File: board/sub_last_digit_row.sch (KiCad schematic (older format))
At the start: 83 parts, among them Q901 Q_PMOS_GSD, Q902 Q_PMOS_GSD, Q903 Q_PMOS_GSD, Q904 Q_PMOS_GSD, Q905 Q_PMOS_GSD, Q906 Q_PMOS_GSD, Q907 Q_PMOS_GSD, Q908 Q_PMOS_GSD, U901 TPIC6D595, U902 TPIC6D595, U903 TPIC6D595

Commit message: More Schematic progress
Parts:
- removed D904: (no value), symbol quokka:14-segment
- removed Q908: Q_PMOS_GSD, symbol Device:Q_PMOS_GSD
- removed R901, R902, R904, R905, R907, R908, R909, R910, R911, R912, R913, R914, R915, R916, R917, R918, R919, R921, R922, R924, R925, R926, R927, R928, R929, R930, R931, R932, R933, R934, R935, R936, R938, R939, R941, R942, R943, R944, R945, R946, R947, R948, R949, R950, R951, R952, R953, R955, R956, R958, R959, R960, R961, R962, R963, R964, R965, R966, R967, R968: 100, symbol Device:R
- removed R957: 4K7, symbol Device:R
- added C801, C802, C803: 1u, symbol Device:C
- added D804, D805, D806, D807, D808, D809, D810, D811, D812, D813, D814, D815, D816, D817, D818, D819: LED_Small, symbol Device:LED_Small
- added R808, R809, R810, R811, R812, R813, R814, R815, R816, R817, R818, R819, R820, R821, R822, R823, R824, R825, R826, R827, R828, R829, R830, R831, R832, R833, R834, R835, R836, R837, R838, R839, R840, R841, R842, R843, R844, R845, R846, R847, R848, R849, R850, R851, R852, R853, R854, R855, R856, R857, R858, R859, R860, R861, R862, R863, R864, R865, R866, R867, R868: 100, symbol Device:R
- renumbered D901 to D801, D902 to D802, D903 to D803, Q901 to Q801, Q902 to Q802, Q903 to Q803, Q904 to Q804, Q905 to Q805, Q906 to Q806, Q907 to Q807, R903 to R801, R906 to R802, R920 to R803, R923 to R804, R937 to R805, R940 to R806, R954 to R807, U901 to U801, U902 to U802, U903 to U803
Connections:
- net +5V: now also C801.1, C802.1, C803.1
- net GND: now also C801.2, C802.2, C803.2
- net at D801.1 (E): now also R808.1
- net at D801.10 (B): now also R816.1
- net at D801.12 (A): now also R817.1
- net at D801.13 (G1): now also R818.1
- net at D801.14 (K): now also R819.1
- net at D801.15 (J): now also R820.1
- net at D801.17 (H): now also R821.1
- net at D801.18 (F): now also R822.1
- net at D801.2 (N): now also R809.1
- net at D801.4 (M): now also R810.1
- net at D801.5 (L): now also R811.1
- net at D801.6 (G2): now also R812.1
- net at D801.7 (D): now also R813.1
- net at D801.8 (DP): now also R814.1
- net at D801.9 (C): now also R815.1
- net at U802.3 (DRAIN0): now also R808.2, R823.2, R838.2, R853.2
- net at U802.4 (DRAIN1): now also R809.2, R824.2, R839.2, R854.2
- net at U802.5 (DRAIN2): now also R810.2, R825.2, R840.2, R855.2
- net at U802.6 (DRAIN3): now also R811.2, R826.2, R841.2, R856.2
- net at U802.11 (DRAIN4): now also R812.2, R827.2, R842.2, R857.2
- net at U802.12 (DRAIN5): now also R813.2, R828.2, R843.2, R858.2
- net at U802.13 (DRAIN6): now also R814.2, R829.2, R844.2, R859.2
- net at U802.14 (DRAIN7): now also R815.2, R830.2, R845.2, R860.2
- net at U803.3 (DRAIN0): now also R816.2, R831.2, R846.2, R861.2
- net at U803.4 (DRAIN1): now also R817.2, R832.2, R847.2, R862.2
- net at U803.5 (DRAIN2): now also R818.2, R833.2, R848.2, R863.2
- net at U803.6 (DRAIN3): now also R819.2, R834.2, R849.2, R864.2
- net at U803.11 (DRAIN4): now also R820.2, R835.2, R850.2, R865.2
- net at U803.12 (DRAIN5): now also R821.2, R836.2, R851.2, R866.2
- net at U803.13 (DRAIN6): now also R822.2, R837.2, R852.2, R867.2
- net at D802.1 (E): now also R823.1
- net at D802.10 (B): now also R831.1
- net at D802.12 (A): now also R832.1
- net at D802.13 (G1): now also R833.1
- net at D802.14 (K): now also R834.1
- net at D802.15 (J): now also R835.1
- net at D802.17 (H): now also R836.1
- net at D802.18 (F): now also R837.1
- net at D802.2 (N): now also R824.1
- net at D802.4 (M): now also R825.1
- net at D802.5 (L): now also R826.1
- net at D802.6 (G2): now also R827.1
- net at D802.7 (D): now also R828.1
- net at D802.8 (DP): now also R829.1
- net at D802.9 (C): now also R830.1
- net at D803.1 (E): now also R838.1
- net at D803.10 (B): now also R846.1
- net at D803.12 (A): now also R847.1
- net at D803.13 (G1): now also R848.1
- net at D803.14 (K): now also R849.1
- net at D803.15 (J): now also R850.1
- net at D803.17 (H): now also R851.1
- net at D803.18 (F): now also R852.1
- net at D803.2 (N): now also R839.1
- net at D803.4 (M): now also R840.1
- net at D803.5 (L): now also R841.1
- net at D803.6 (G2): now also R842.1
- net at D803.7 (D): now also R843.1
- net at D803.8 (DP): now also R844.1
- net at D803.9 (C): now also R845.1
- net at Q807.2 (S): now also D804.2 (A), D805.2 (A), D806.2 (A), D807.2 (A), D808.2 (A), D809.2 (A), D810.2 (A), D811.2 (A), D812.2 (A), D813.2 (A), D814.2 (A), D815.2 (A), D816.2 (A), D817.2 (A), D818.2 (A), D819.2 (A)
- net at U803.14 (DRAIN7): now also R868.2
- net at U801.3 (DRAIN0): now also Q807.1 (G), R807.2, U801.4 (DRAIN1)
- new net: D804.1 (K), R853.1
- new net: D805.1 (K), R854.1
- new net: D806.1 (K), R855.1
- new net: D807.1 (K), R856.1
- new net: D808.1 (K), R857.1
- new net: D809.1 (K), R858.1
- new net: D810.1 (K), R859.1
- new net: D811.1 (K), R860.1
- new net: D812.1 (K), R861.1
- new net: D813.1 (K), R862.1
- new net: D814.1 (K), R863.1
- new net: D815.1 (K), R864.1
- new net: D816.1 (K), R865.1
- new net: D817.1 (K), R866.1
- new net: D818.1 (K), R867.1
- new net: D819.1 (K), R868.1
- no-connect marks 0 -> 1
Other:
- moved on the sheet: D801, D802, D803, Q801, Q802, Q803, Q804, Q805, Q806, Q807, R801, R802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

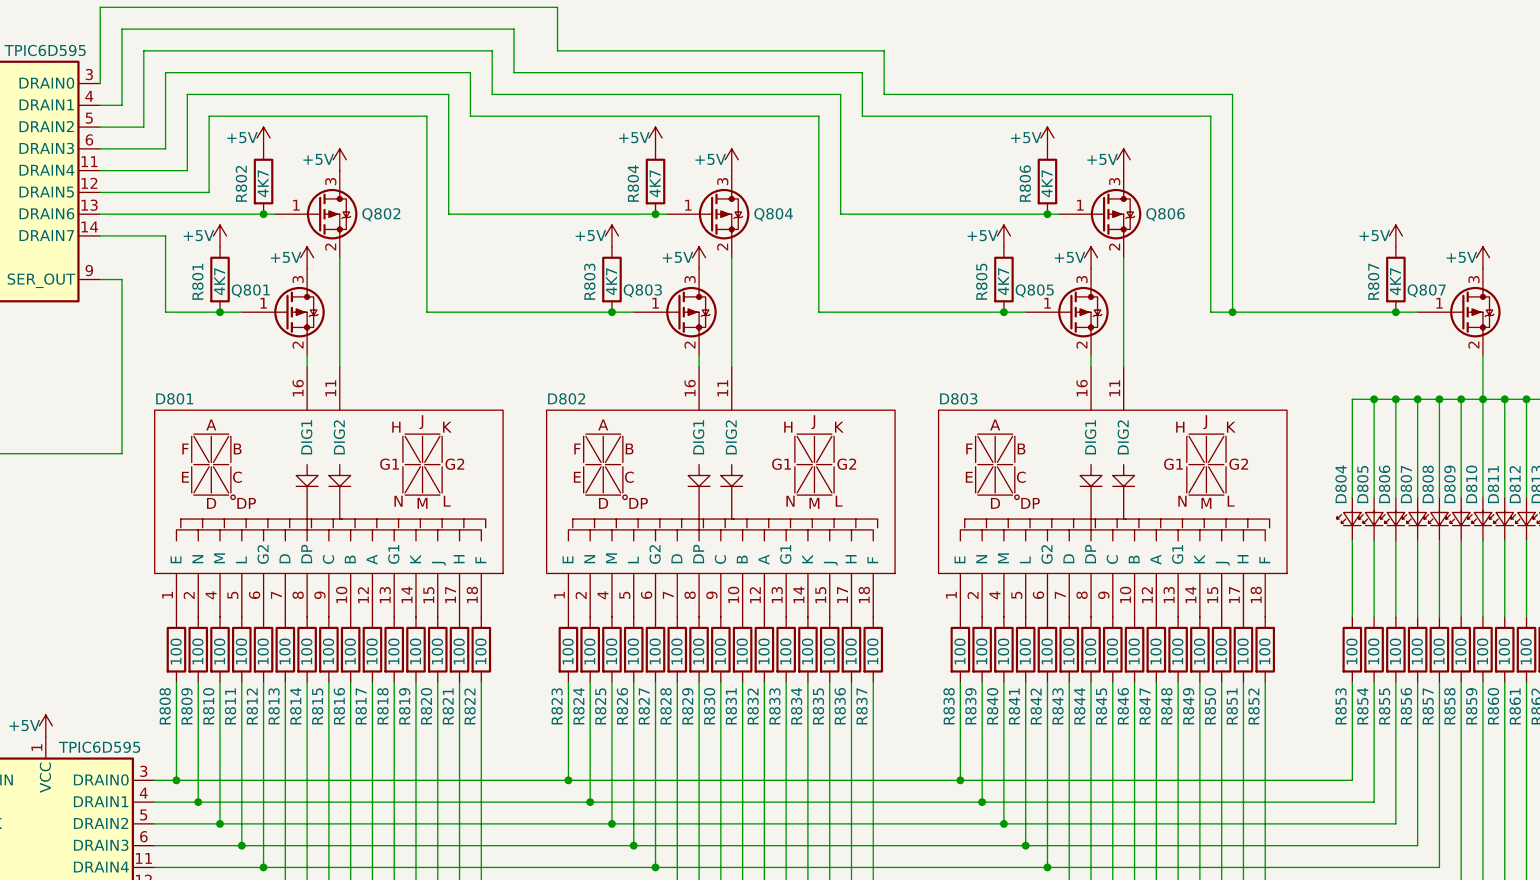
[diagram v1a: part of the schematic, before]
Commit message: Bus signal connectivity rebuilt
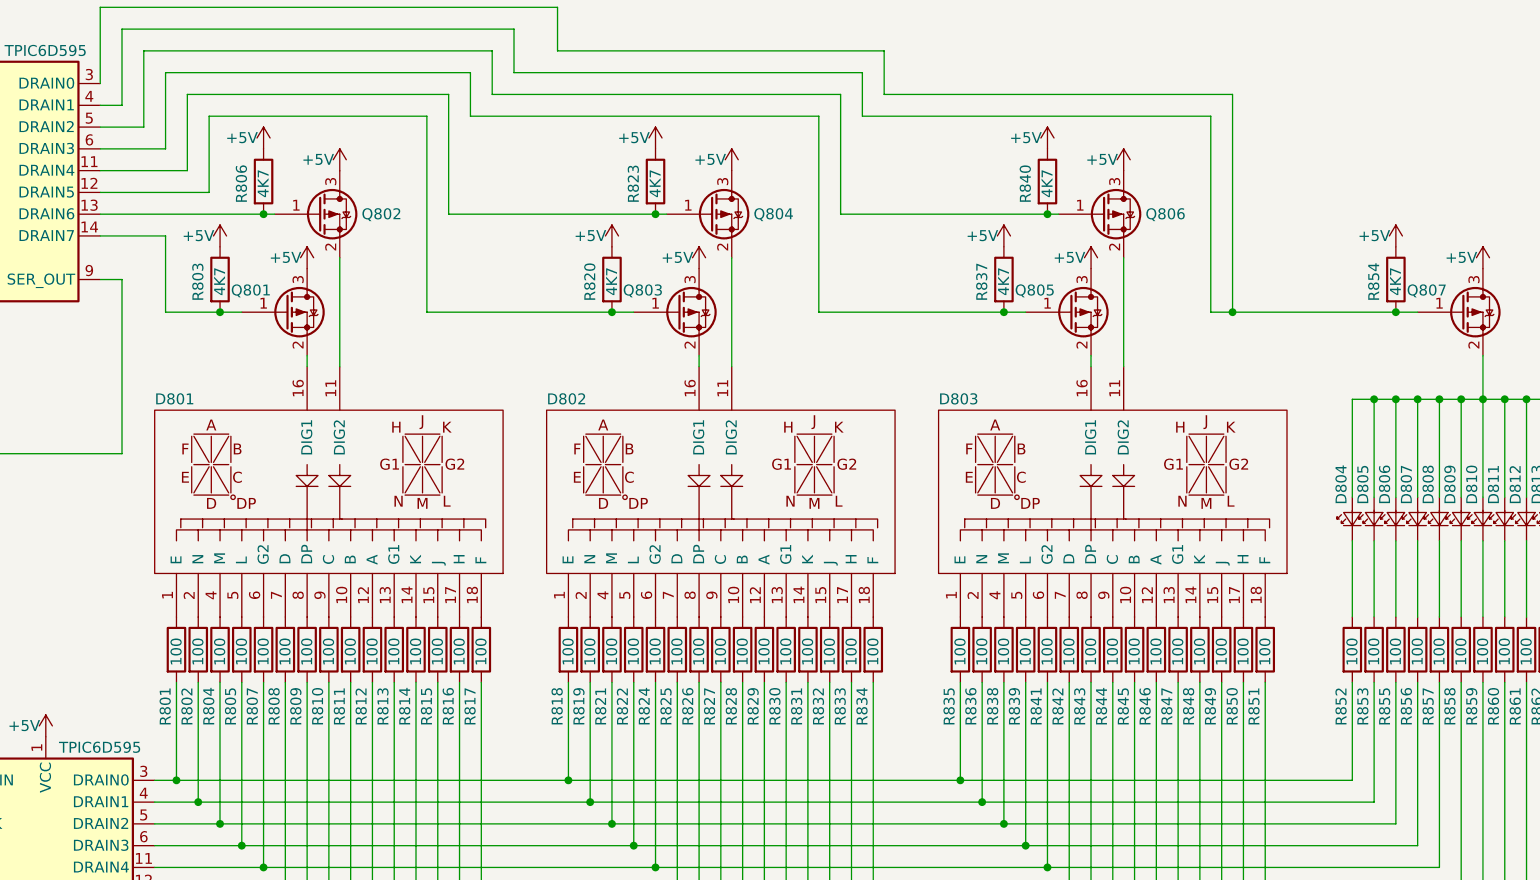
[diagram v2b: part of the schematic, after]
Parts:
- renumbered R808 to R801, R809 to R802, R801 to R803, R810 to R804, R811 to R805, R802 to R806, R812 to R807, R813 to R808, R814 to R809, R815 to R810, R816 to R811, R817 to R812, R818 to R813, R819 to R814, R820 to R815, R821 to R816, R822 to R817, R823 to R818, R824 to R819, R803 to R820, R825 to R821, R826 to R822, R804 to R823, R827 to R824, R828 to R825, R829 to R826, R830 to R827, R831 to R828, R832 to R829, R833 to R830, R834 to R831, R835 to R832, R836 to R833, R837 to R834, R838 to R835, R839 to R836, R805 to R837, R840 to R838, R841 to R839, R806 to R840, R842 to R841, R843 to R842, R844 to R843, R845 to R844, R846 to R845, R847 to R846, R848 to R847, R849 to R848, R850 to R849, R851 to R850, R852 to R851, R853 to R852, R854 to R853, R807 to R854

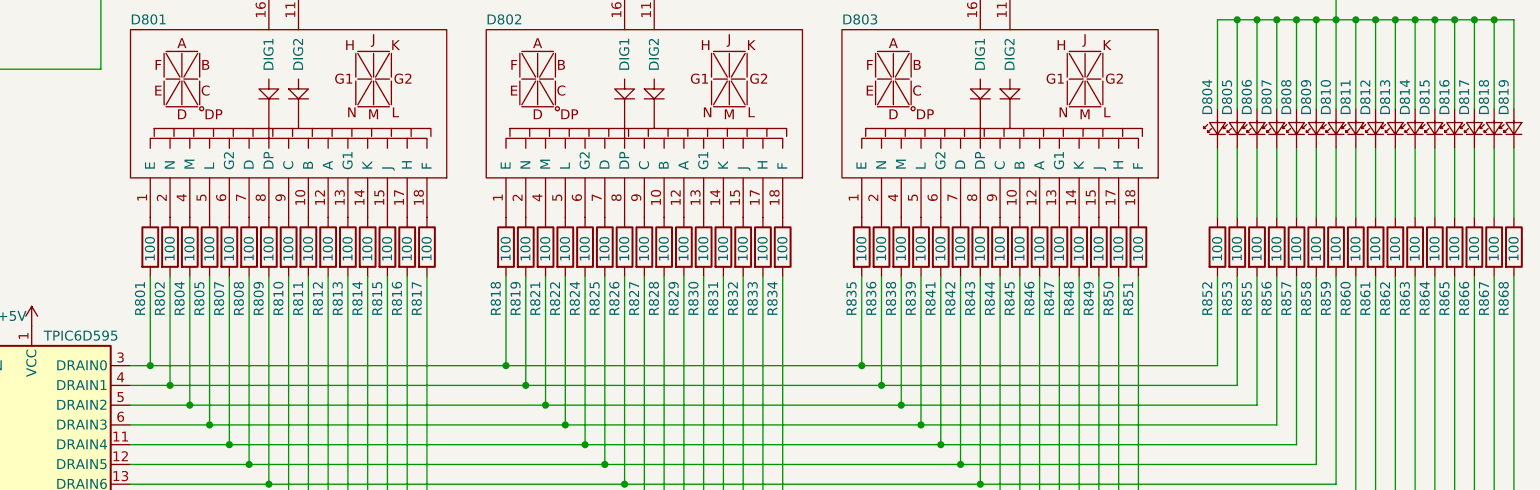
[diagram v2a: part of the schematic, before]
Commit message: made some changes based on projected power budget
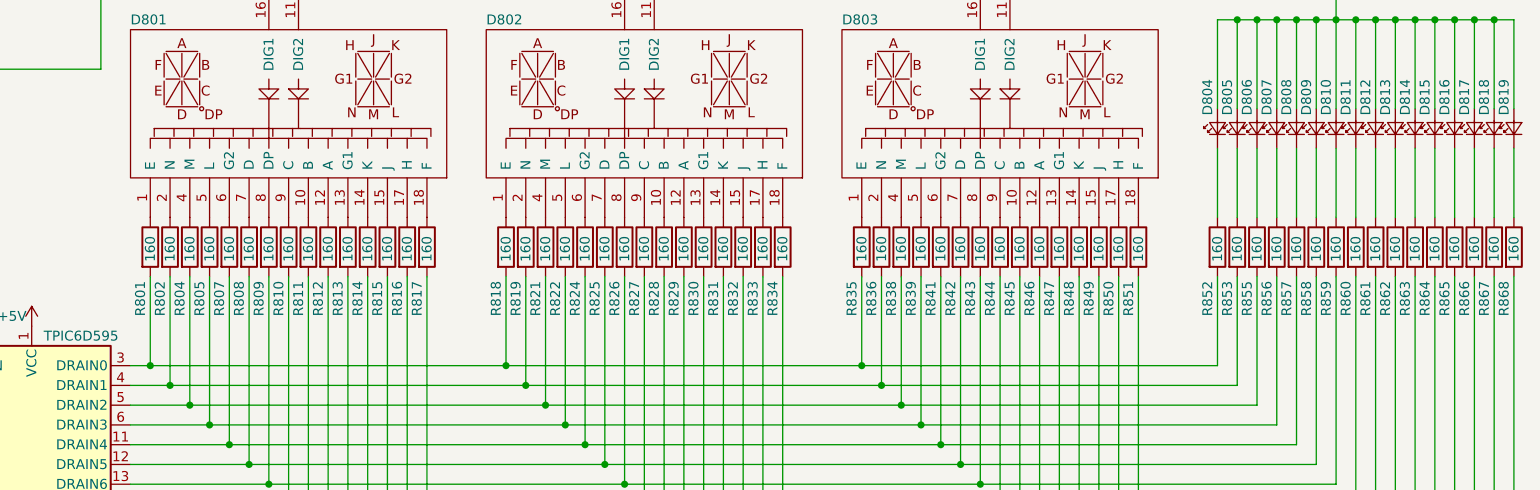
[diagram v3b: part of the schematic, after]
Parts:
- R801, R802, R804, R805, R807, R808, R809, R810, R811, R812, R813, R814, R815, R816, R817, R818, R819, R821, R822, R824, R825, R826, R827, R828, R829, R830, R831, R832, R833, R834, R835, R836, R838, R839, R841, R842, R843, R844, R845, R846, R847, R848, R849, R850, R851, R852, R853, R855, R856, R857, R858, R859, R860, R861, R862, R863, R864, R865, R866, R867, R868: value 100 -> 160

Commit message: Schematics mostly complete
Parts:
- renumbered D804 to D801, D805 to D802, D806 to D803, D807 to D804, D808 to D805, D809 to D806, D810 to D807, D811 to D808, D812 to D809, D813 to D810, D814 to D811, D815 to D812, D816 to D813, D817 to D814, D818 to D815, D819 to D816, D801 to D817, D802 to D818, D803 to D819, Q802 to Q801, Q804 to Q802, Q806 to Q803, Q801 to Q804, Q803 to Q805, Q805 to Q806, R806 to R801, R823 to R802, R840 to R803, R803 to R804, R820 to R805, R837 to R806, R854 to R807, R852 to R808, R853 to R809, R855 to R810, R856 to R811, R857 to R812, R858 to R813, R859 to R814, R860 to R815, R861 to R816, R862 to R817, R863 to R818, R864 to R819, R865 to R820, R866 to R821, R867 to R822, R868 to R823, R801 to R824, R802 to R825, R804 to R826, R805 to R827, R807 to R828, R808 to R829, R809 to R830, R810 to R831, R811 to R832, R812 to R833, R813 to R834, R814 to R835, R815 to R836, R816 to R837, R817 to R838, R818 to R839, R819 to R840, R821 to R841, R822 to R842, R824 to R843, R825 to R844, R826 to R845, R827 to R846, R828 to R847, R829 to R848, R830 to R849, R831 to R850, R832 to R851, R833 to R852, R834 to R853, R835 to R854, R836 to R855, R838 to R856, R839 to R857, R841 to R858, R842 to R859, R843 to R860, R844 to R861, R845 to R862, R846 to R863, R847 to R864, R848 to R865, R849 to R866, R850 to R867, R851 to R868
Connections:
- net at R808.2, R824.2, R839.2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: now also R809.2, R810.2, R811.2, R812.2, R813.2, R814.2, R815.2, R816.2, R817.2, R818.2, R819.2, R820.2, R821.2, R822.2, R825.2, R826.2, R827.2, R828.2, R829.2, R830.2, R831.2, R832.2, R833.2, R834.2, R835.2, R836.2, R837.2, R838.2, R840.2, R841.2, R842.2, R843.2, R844.2, R845.2, R846.2, R847.2, R848.2, R849.2, R850.2, R851.2, R852.2, R853.2, R855.2, R856.2, R857.2, R858.2, R859.2, R860.2, R861.2, R862.2, R863.2, R864.2, R865.2, R866.2, R867.2, R868.2, U802.11 (DRAIN4), U802.12 (DRAIN5), U802.13 (DRAIN6), U802.14 (DRAIN7), U802.4 (DRAIN1), U802.5 (DRAIN2), U802.6 (DRAIN3), U803.11 (DRAIN4), U803.12 (DRAIN5), U803.13 (DRAIN6), U803.3 (DRAIN0), U803.4 (DRAIN1), U803.5 (DRAIN2), U803.6 (DRAIN3)
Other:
- moved on the sheet: R824, R825, R826, R827, R828, R829, R830, R831, R832, R833, R834, R835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
